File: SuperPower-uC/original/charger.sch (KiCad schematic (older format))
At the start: 30 parts, among them J2 DNP/JST_ZH_S2B_thru, J3 DNP/JST_XH_S2B_thru, Q2 DMN3018SSD, Q3 2N7002A, Q4 DMP3028LSD, U2 LTC4162EUFD-LAD

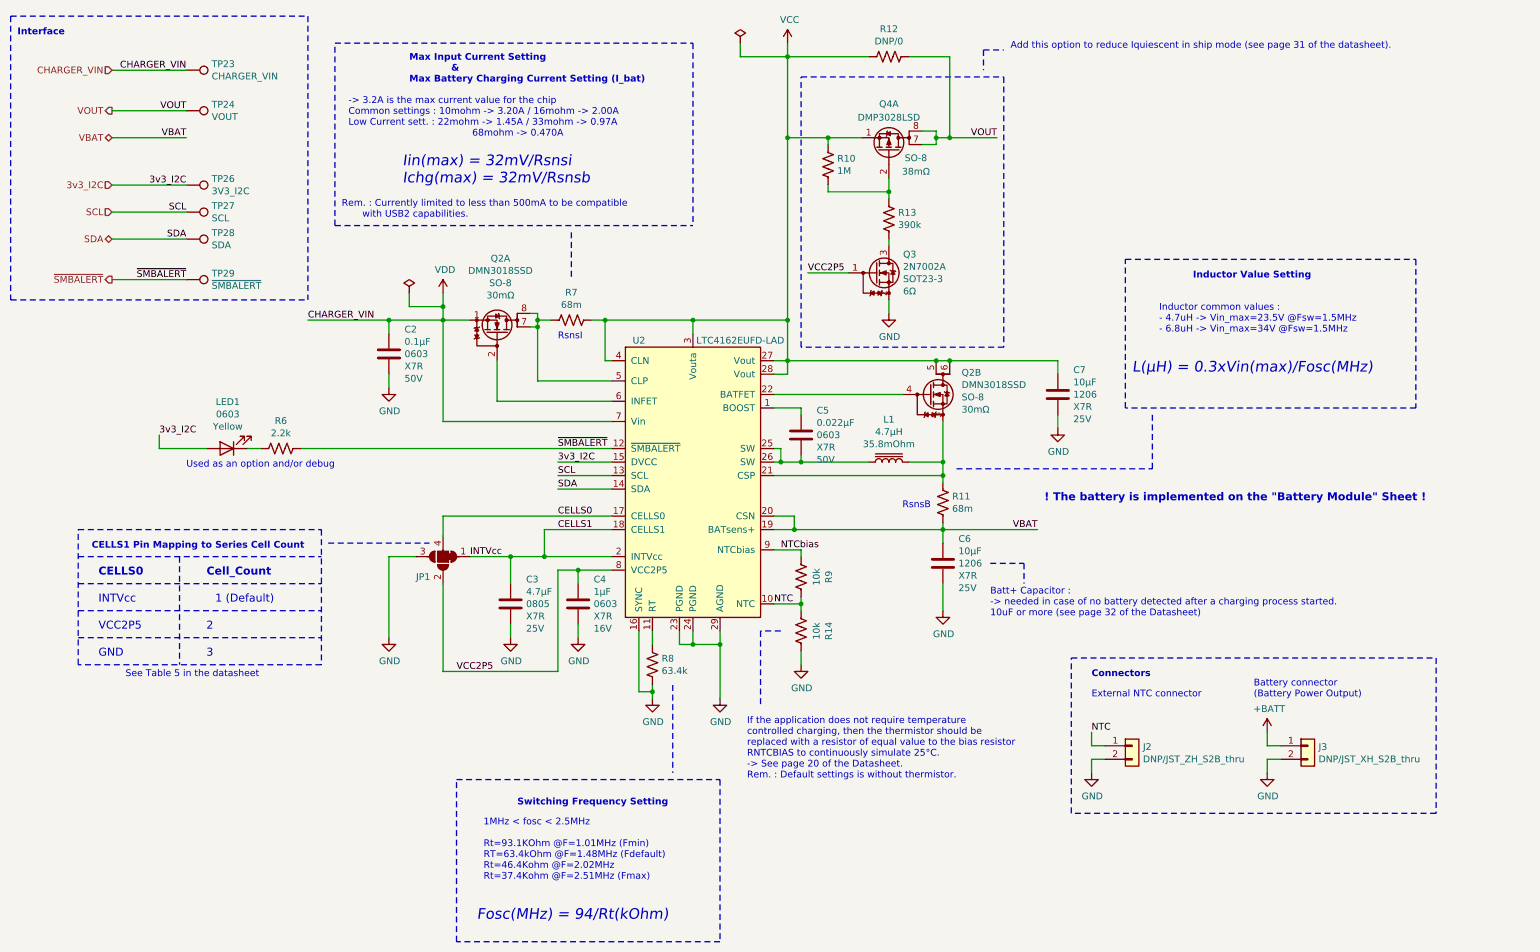
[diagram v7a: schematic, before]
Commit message: Update "Charger Sheet" components
IC, Capacitors, Inductor and Connectors + Misc. Text
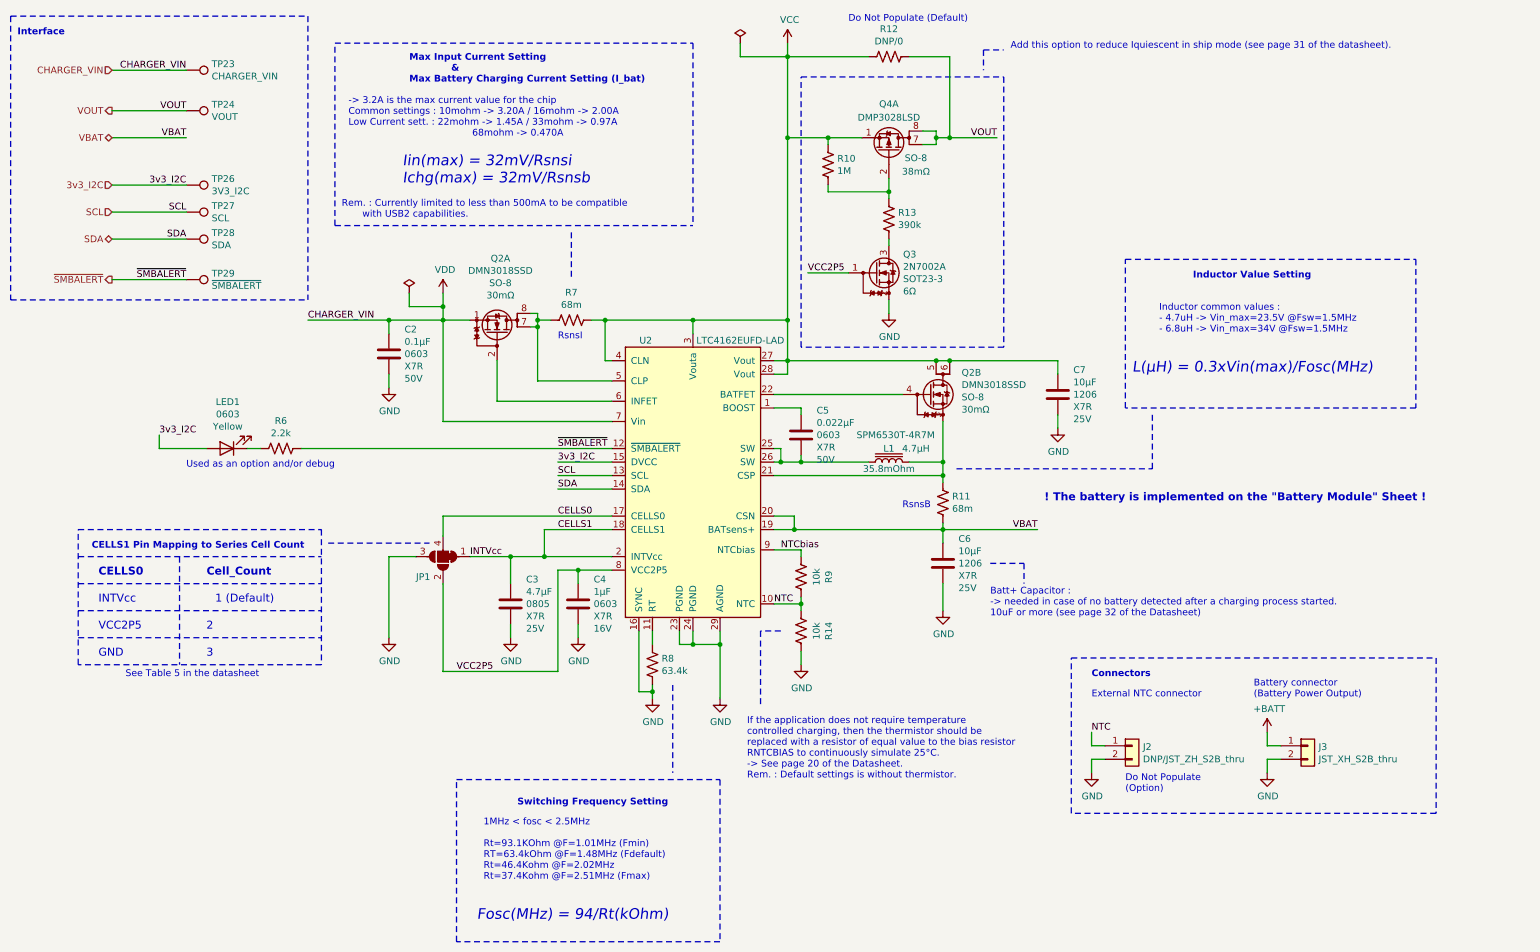
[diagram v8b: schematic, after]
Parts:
- C2: footprint Capacitor_SMD:C_0805_2012Metric -> Capacitor_SMD:C_0603_1608Metric; Farnell_price_qt=1 (none) -> -; Farnell_price_qt=500 0.0221€ -> (none); LCSC_price_qt=1 (none) -> -; LCSC_price_qt=10 (none) -> -; LCSC_price_qt=100 (none) -> $0.0093; LCSC_price_qt=1000 (none) -> $0.0069; LCSC_price_qt=1500 $0.0065 -> (none); LCSC_price_qt=50 $0.0093 -> (none); LCSC_price_qt=500 $0.0069 -> (none); LCSC_price_qt=5000 $0.0061 -> (none); RS_price_qt=1 (none) -> -; RS_price_qt=10 (none) -> -; RS_price_qt=100 (none) -> 0.025€; RS_price_qt=200 0.025€ -> (none); RS_price_qt=2000 0.017€ -> (none); Release_date 2020-11-27 -> 2020-12-12; Release_version 1.00 -> 1.02
- C3: Farnell_price_qt=1 (none) -> -; Farnell_price_qt=10 (none) -> -; Farnell_price_qt=100 (none) -> -; Farnell_price_qt=1000 (none) -> 0,0625 € (QT=3000); Farnell_price_qt=250 - -> (none); Farnell_price_qt=3000 0,0625 € -> (none); Farnell_price_qt=500 - -> (none); Farnell_price_qt=6000 0,0529 € -> (none); LCSC_price_qt=1 (none) -> -; LCSC_price_qt=10 (none) -> -; LCSC_price_qt=100 (none) -> $0.035; LCSC_price_qt=1000 (none) -> $0.025; LCSC_price_qt=20 $0.035 -> (none); LCSC_price_qt=200 $0.0266 -> (none); LCSC_price_qt=2000 $0.02 -> (none); LCSC_price_qt=600 $0.025 -> (none); Mouser_price_qt=1000 (none) -> $0.086; Mouser_price_qt=500 $0.098 -> (none); RS_price_qt=1 (none) -> -; RS_price_qt=10 (none) -> -; RS_price_qt=100 (none) -> 0,118 €; RS_price_qt=1000 (none) -> 0,069 €; RS_price_qt=200 0,098 € -> (none); RS_price_qt=50 0,118 € -> (none); RS_price_qt=800 0,069 € -> (none); Release_date 2020-11-29 -> 2020-12-12; Release_version 1.00 -> 1.01
- C4: Farnell_price_qt=1 (none) -> -; Farnell_price_qt=500 0,0189 € -> (none); LCSC_price_qt=1 (none) -> -; LCSC_price_qt=10 (none) -> -; LCSC_price_qt=100 (none) -> $0.0051; LCSC_price_qt=1000 (none) -> $0.0037; LCSC_price_qt=1500 $0.0034 -> (none); LCSC_price_qt=50 $0.0051 -> (none); LCSC_price_qt=500 $0.0037 -> (none); LCSC_price_qt=5000 $0.0032 -> (none); Mouser_price_qt=1 $0.101 -> $0.101; Mouser_price_qt=10 $0.05 -> $0.050; Mouser_price_qt=1000 (none) -> $0.012; Mouser_price_qt=500 $0.015 -> (none); RS_price_qt=1 (none) -> -; RS_price_qt=10 (none) -> -; RS_price_qt=100 (none) -> -; RS_price_qt=1000 (none) -> 0,008 € (QT=4000); RS_price_qt=4000 0,008 € -> (none); RS_price_qt=8000 0,008 € -> (none)
- C5: Farnell_price_qt=1 (none) -> -; Farnell_price_qt=500 0,0148 € -> (none); LCSC_price_qt=1 (none) -> -; LCSC_price_qt=10 (none) -> -; LCSC_price_qt=100 (none) -> $0.0065; LCSC_price_qt=1000 (none) -> $0.0047; LCSC_price_qt=1500 $0.0043 -> (none); LCSC_price_qt=50 $0.0065 -> (none); LCSC_price_qt=500 $0.0047 -> (none); LCSC_price_qt=5000 $0.004 -> (none); Mfr_name (none) -> Samsung; Mouser_price_qt=1000 (none) -> $0.010; Mouser_price_qt=500 $0.012 -> (none); RS_price_qt=1 (none) -> -; RS_price_qt=10 (none) -> -; RS_price_qt=100 (none) -> -; RS_price_qt=1000 (none) -> 0,006 € (QT=4000); RS_price_qt=4000 0,006 € -> (none); Release_date 2020-11-29 -> 2020-12-12; Release_version 1.00 -> 1.01
- C6, C7: Farnell_price_qt=1 (none) -> -; Farnell_price_qt=10 (none) -> 0,227 €; Farnell_price_qt=100 (none) -> 0,105 €; Farnell_price_qt=1000 (none) -> 0,0579 €; Farnell_price_qt=250 0,0857 € -> (none); Farnell_price_qt=5 0,227 € -> (none); Farnell_price_qt=50 0,105 € -> (none); Farnell_price_qt=500 0,0663 € -> (none); LCSC_price_qt=1 (none) -> -; LCSC_price_qt=300 $0.0263 -> (none); Mouser_price_qt=1000 (none) -> $0.058; Mouser_price_qt=500 $0.067 -> (none); RS_price_qt=1 (none) -> -; RS_price_qt=10 (none) -> -; RS_price_qt=100 (none) -> -; RS_price_qt=1000 (none) -> 0,048 € (QT=2000); RS_price_qt=10000 0,045 € -> (none); RS_price_qt=2000 0,048 € -> (none); RS_price_qt=6000 0,046 € -> (none); Release_date 2020-11-28 -> 2020-12-12; Release_version 1.00 -> 1.01
- J2: footprint JST_ZH_S2B_THRU:JST_ZH_S2B-ZR_1x02_P1.50mm_Horizontal -> Connector_JST_user:JST_ZH_S2B-ZR_1x02_P1.50mm_Horizontal; LCSC_price_qt=1 (none) -> -; LCSC_price_qt=300 $0.034 -> (none); Mouser_price_qt=1 (none) -> -; Mouser_price_qt=10 (none) -> -; Mouser_price_qt=100 (none) -> -; Mouser_price_qt=1000 (none) -> -; Mouser_stock (none) -> 4300; RS_price_qt=1 (none) -> -; RS_price_qt=10 (none) -> 0.484€; RS_price_qt=100 (none) -> 0.484€; RS_price_qt=1000 (none) -> 0.364€; RS_price_qt=125 0.396€ -> (none); RS_price_qt=2500 0.338€ -> (none); RS_price_qt=5 0.484€ -> (none); RS_price_qt=500 0.364€ -> (none); Release_date 2020-11-25 -> 2020-12-12; Release_version 1.00 -> 1.01
- J3: value DNP/JST_XH_S2B_thru -> JST_XH_S2B_thru; footprint Connector_JST:JST_XH_S2B-XH-A-1_1x02_P2.50mm_Horizontal -> Connector_JST:JST_XH_S2B-XH-A_1x02_P2.50mm_Horizontal; Farnell_price_qt=1 (none) -> -; Farnell_price_qt=10 (none) -> -; LCSC_price_qt=1 (none) -> -; LCSC_price_qt=300 $0.038 -> (none); Mouser_price_qt=1 (none) -> -; Mouser_price_qt=10 (none) -> -; Mouser_price_qt=100 (none) -> -; Mouser_price_qt=1000 (none) -> -; Mouser_stock (none) -> -; RS_price_qt=1 (none) -> -; RS_price_qt=10 (none) -> 0.43€; RS_price_qt=100 (none) -> -; RS_price_qt=1000 (none) -> 0.108€; RS_price_qt=125 0.116€ -> (none); RS_price_qt=1250 0.104€ -> (none); RS_price_qt=5 0.43€ -> (none); RS_price_qt=500 0.108€ -> (none); Release_date 2020-11-24 -> 2020-12-12; Release_version 1.00 -> 1.01
- L1: footprint Inductor_SMD_user:L_TDK_SPM6530T -> SPM6530T-4R7M:L_TDK_SPM6530T; Farnell_price_qt=10 (none) -> 1,36 €; Farnell_price_qt=1000 (none) -> 0,454 €; Farnell_price_qt=250 0,659 € -> (none); Farnell_price_qt=50 0,785 € -> (none); LCSC_price_qt=1000 (none) -> $0.0955; LCSC_price_qt=30 $0.1078 -> (none); Mouser_price_qt=1000 (none) -> $0.564; Mouser_price_qt=500 $0.601 -> (none); RS_price_qt=1 (none) -> -; RS_price_qt=10 (none) -> 1,224 €; RS_price_qt=100 0,794 € -> 0,92 €; RS_price_qt=1000 (none) -> 0,734 €; RS_price_qt=25 1,038 € -> (none); RS_price_qt=5 1,224 € -> (none); RS_price_qt=50 0,92 € -> (none); Release_date 2020-12-02 -> 2020-12-12; Release_version 1.00 -> 1.01
- U2: Designer (none) -> ManWithNoName; Farnell_check_date (none) -> 2020-11-22; Farnell_price_qt=1 (none) -> -; Farnell_price_qt=10 (none) -> -; Farnell_price_qt=100 (none) -> -; Farnell_price_qt=1000 (none) -> -; Farnell_stock (none) -> -; LCSC_check_date (none) -> 2020-12-12; LCSC_price_qt=1 (none) -> $11.892; LCSC_price_qt=10 (none) -> $11.892; LCSC_price_qt=100 (none) -> $11.892; LCSC_price_qt=1000 (none) -> $4.3605; LCSC_stock (none) -> 0; Mfr_name (none) -> Analog Devices; Mfr_no (none) -> LTC4162EUFD-LAD#PBF; Mouser_check_date (none) -> 2020-12-12; Mouser_link https://www.mouser.fr/ProductDetail/Analog-Devices/LTC4162E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 -> https://eu.mouser.com/ProductDetail/Analog-Devices/LTC4162E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; Mouser_price_qt=1 (none) -> $7.39; Mouser_price_qt=10 (none) -> $7.39; Mouser_price_qt=100 (none) -> $3.90; Mouser_price_qt=1000 (none) -> $3.75; Mouser_stock (none) -> 568 (438 Expected 07/16/2021); Package (none) -> QFN-28 (2.65x3.65mm); RS_check_date (none) -> 2020-12-12; RS_price_qt=1 (none) -> -; RS_price_qt=10 (none) -> -; RS_price_qt=100 (none) -> -; RS_price_qt=1000 (none) -> -; RS_stock (none) -> -; Release_date (none) -> 2020-12-12; Release_version (none) -> 1.01; Status (none) -> TO_CHECK
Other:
- note added: "Do Not Populate (Default)"
- note added: "Do Not Populate\n(Option)"
